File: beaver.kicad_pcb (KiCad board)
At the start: 2 copper layers, 74.3 x 27.3 mm, 10 parts, among them J1 BOARD_FTDI, J3 FTDI

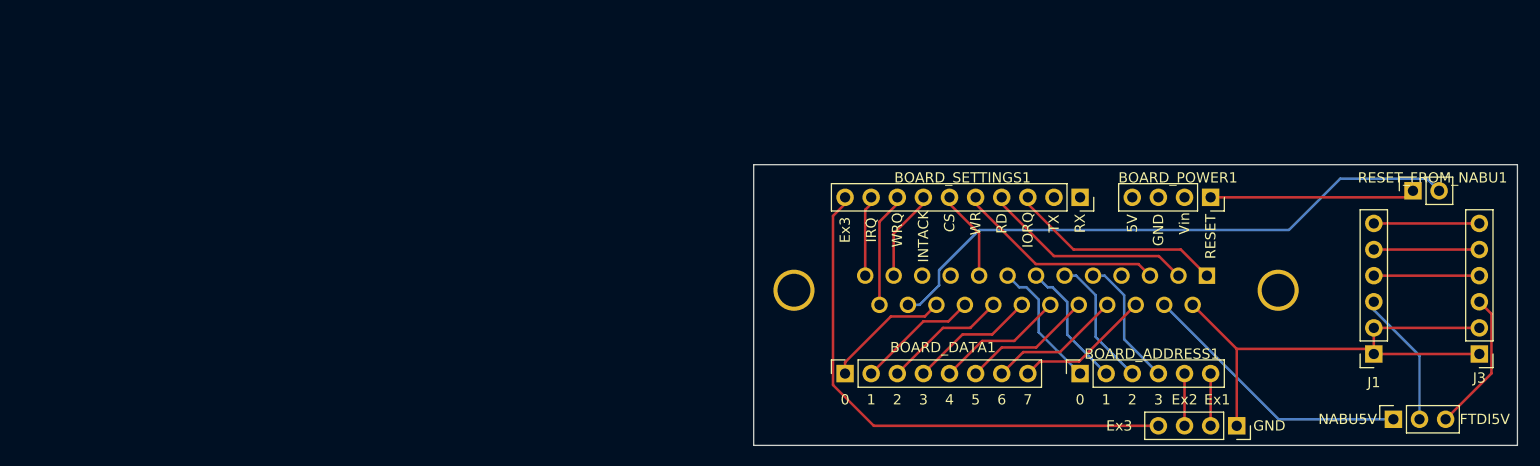
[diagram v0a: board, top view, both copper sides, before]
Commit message: Boarduino pinout was wrong for 4 pins. Will need to drop support for WAIT_REQUEST.
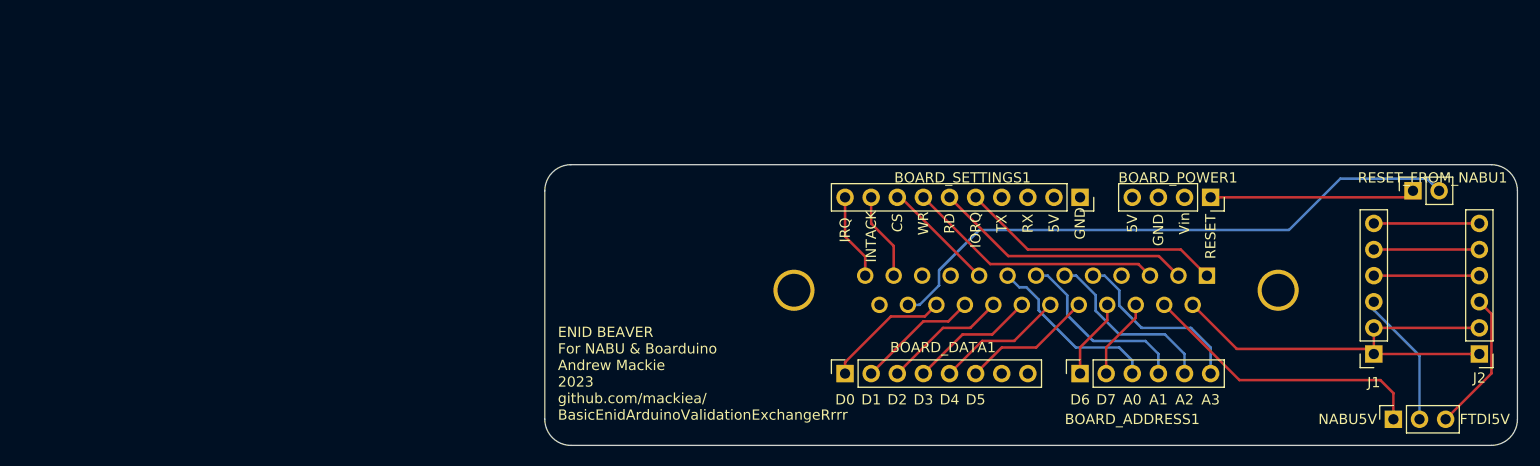
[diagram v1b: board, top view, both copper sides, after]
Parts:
- removed BOARD_EXTRA1: Conn_01x03_Male, Connector_PinSocket_2.54mm:PinSocket_1x04_P2.54mm_Vertical
- renumbered J3 to J2
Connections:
- net Net-(BOARD_SETTINGS1-Pad1) renamed GND_UNUSED1
- net Net-(BOARD_SETTINGS1-Pad2) renamed 5V_UNUSED
- BOARD_ADDRESS1 pad 1: ADDRESS_0 -> DATA_6
- BOARD_ADDRESS1 pad 2: ADDRESS_1 -> DATA_7
- BOARD_ADDRESS1 pad 3: ADDRESS_2 -> ADDRESS_0
- BOARD_ADDRESS1 pad 4: ADDRESS_3 -> ADDRESS_1
- BOARD_ADDRESS1 pad 5: Net-(BOARD_ADDRESS1-Pad5) -> ADDRESS_2
- BOARD_ADDRESS1 pad 6: Net-(BOARD_ADDRESS1-Pad6) -> ADDRESS_3
- BOARD_DATA1 pad 7: DATA_6 -> GND_UNUSED2
- BOARD_DATA1 pad 8: DATA_7 -> AREF
- BOARD_SETTINGS1 pad 10: Net-(BOARD_EXTRA1-Pad4) -> INTERRUPT_REQUEST
- BOARD_SETTINGS1 pad 3: IO_REQUEST -> ARDUINO_READ
- BOARD_SETTINGS1 pad 4: READ -> ARDUINO_WRITE
- BOARD_SETTINGS1 pad 5: WRITE -> IO_REQUEST
- BOARD_SETTINGS1 pad 6: CARD_SELECT -> READ
- BOARD_SETTINGS1 pad 7: INTERRUPT_ACKNOWLEDGE -> WRITE
- BOARD_SETTINGS1 pad 8: WAIT_REQUEST -> CARD_SELECT
- BOARD_SETTINGS1 pad 9: INTERRUPT_REQUEST -> INTERRUPT_ACKNOWLEDGE
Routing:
- net Net-(BOARD_EXTRA1-Pad4): track 51.4 -> 0.00 mm
- net WAIT_REQUEST: track 10.5 -> 0.00 mm
- net GROUND_1: track 50.1 -> 42.7 mm
- net ADDRESS_1: track 12.6 -> 18.1 mm
- net DATA_7: track 13.3 -> 7.88 mm
- net IO_REQUEST: track 20.3 -> 25.7 mm
- net WRITE: track 19.9 -> 25.2 mm
- net READ: track 20.1 -> 25.4 mm
- net DATA_6: track 13.0 -> 7.78 mm
- net Net-(BOARD_ADDRESS1-Pad6): track 5.08 -> 0.00 mm
- net Net-(BOARD_ADDRESS1-Pad5): track 5.08 -> 0.00 mm
- net ADDRESS_3: track 12.8 -> 17.7 mm
- net ADDRESS_2: track 12.9 -> 17.6 mm
- net ADDRESS_0: track 12.9 -> 17.4 mm
- net CARD_SELECT: track 8.18 -> 11.1 mm
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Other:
- board size 74.3 x 27.3 mm -> 94.6 x 27.3 mm
- board text added: "A0"
- board text added: "A1"
- board text added: "A2"
- board text added: "A3"
- board text added: "D0"
- board text added: "D1"
- board text added: "D2"
- board text added: "D3"
- board text added: "D4"
- board text added: "D5"
- board text added: "D6"
- board text added: "D7"
- board text added: "ENID BEAVER For NABU & Boarduino Andrew Mackie 2023 github.com/mackiea/ BasicEnidArduinoValidationExchangeRrrr"
- board text removed: "0"
- board text removed: "1"
- board text removed: "2"
- board text removed: "3"
- board text removed: "4"
- board text removed: "5"
- board text removed: "6"
- board text removed: "7"
- board text removed: "Ex1"
- board text removed: "Ex2"
- board text removed: "Ex3"
- board text removed: "WRQ"

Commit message: Corrected ENID's DB-25 orientation.
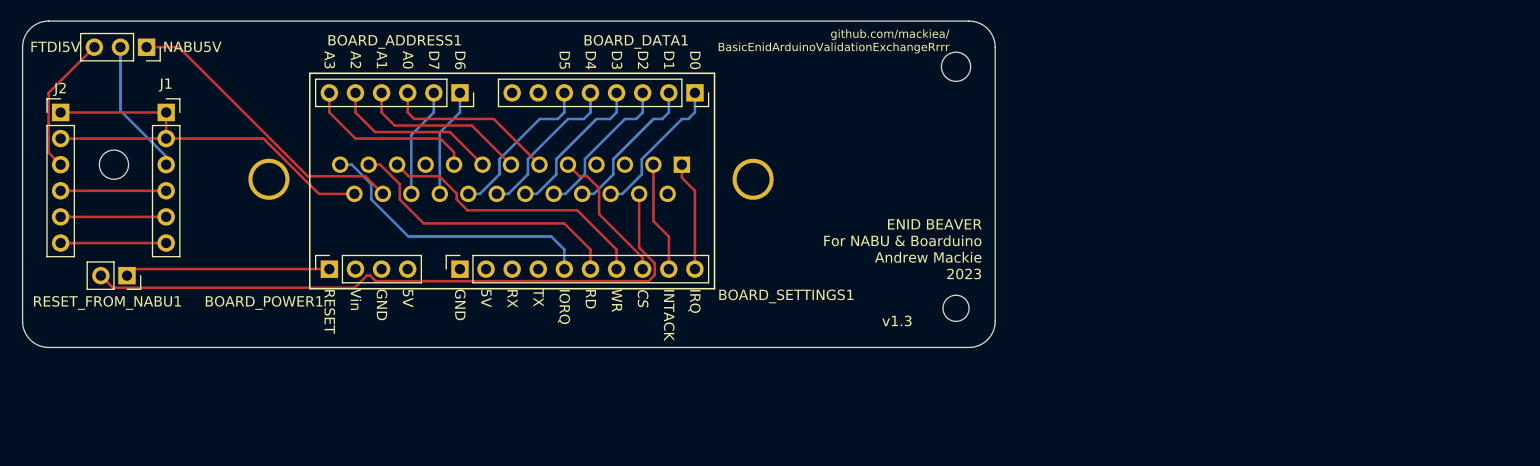
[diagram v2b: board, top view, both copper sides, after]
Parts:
- moved J2 140.0 mm to (38.0, 109.2), turned to 0 degrees
- moved POWER_FROM_ENID_OR_FTDI1 126.6 mm to (46.4, 102.9), turned to 270 degrees
- moved RESET_FROM_NABU1 125.4 mm to (44.5, 125.1), turned to 270 degrees
- moved J1 119.8 mm to (48.3, 109.2), turned to 0 degrees
- moved BOARD_POWER1 86.0 mm to (64.1, 124.5), turned to 90 degrees
- moved BOARD_ADDRESS1 66.2 mm to (76.8, 107.3), turned to 270 degrees
- moved BOARD_SETTINGS1 60.7 mm to (76.8, 124.5), turned to 90 degrees
- moved ENID1 52.2 mm to (98.4, 114.3)
- moved BOARD_DATA1 31.0 mm to (99.7, 107.3), turned to 270 degrees
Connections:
- ENID1 pad 1: IO_REQUEST -> INTERRUPT_REQUEST
- ENID1 pad 10: AUDIO -> 1.79MhzClock
- ENID1 pad 11: 3.58MhzClock -> WRITE
- ENID1 pad 12: INTERRUPT_ACKNOWLEDGE -> READ
- ENID1 pad 13: INTERRUPT_REQUEST -> IO_REQUEST
- ENID1 pad 14: GROUND_1 -> WAIT_REQUEST
- ENID1 pad 15: +5V_1 -> RESET
- ENID1 pad 16: DATA_7 -> DATA_0
- ENID1 pad 17: DATA_6 -> DATA_1
- ENID1 pad 18: DATA_5 -> DATA_2
- ENID1 pad 19: DATA_4 -> DATA_3
- ENID1 pad 2: READ -> INTERRUPT_ACKNOWLEDGE
- ENID1 pad 20: DATA_3 -> DATA_4
- ENID1 pad 21: DATA_2 -> DATA_5
- ENID1 pad 22: DATA_1 -> DATA_6
- ENID1 pad 23: DATA_0 -> DATA_7
- ENID1 pad 24: RESET -> +5V_1
- ENID1 pad 25: WAIT_REQUEST -> GROUND_1
- ENID1 pad 3: WRITE -> 3.58MhzClock
- ENID1 pad 4: 1.79MhzClock -> AUDIO
- ENID1 pad 5: ADDRESS_3 -> CARD_SELECT
- ENID1 pad 6: ADDRESS_2 -> ADDRESS_0
- ENID1 pad 8: ADDRESS_0 -> ADDRESS_2
- ENID1 pad 9: CARD_SELECT -> ADDRESS_3
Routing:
- net RESET: track 58.1 -> 63.8 mm
- net DATA_7: track 7.88 -> 10.7 mm
- net DATA_6: track 7.78 -> 10.6 mm
- net DATA_4: track 12.6 -> 15.2 mm
- net DATA_2: track 12.1 -> 14.7 mm
- net DATA_3: track 12.3 -> 14.9 mm
- net DATA_1: track 11.9 -> 14.5 mm
- net DATA_5: track 12.8 -> 15.4 mm
- net CARD_SELECT: track 11.1 -> 13.6 mm
- net READ: track 25.4 -> 27.8 mm
- net IO_REQUEST: track 25.7 -> 28.0 mm
- net INTERRUPT_ACKNOWLEDGE: track 8.53 -> 10.8 mm
- net INTERRUPT_REQUEST: track 8.43 -> 10.7 mm
- net DATA_0: track 12.3 -> 14.2 mm
- net WRITE: track 25.2 -> 27.0 mm
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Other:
- board size 94.6 x 27.3 mm -> 94.6 x 31.8 mm
- board text added: "ENID BEAVER For NABU & Boarduino Andrew Mackie 2023"
- board text added: "github.com/mackiea/ BasicEnidArduinoValidationExchangeRrrr"
- board text added: "v1.3"
- board text removed: "ENID BEAVER For NABU & Boarduino Andrew Mackie 2023 github.com/mackiea/ BasicEnidArduinoValidationExchangeRrrr"
